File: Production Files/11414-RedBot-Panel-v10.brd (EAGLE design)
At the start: 94 x 49.5 mm, 66 parts, among them U1 ATMEGA328P, U2 TB6612FNG, U3 MIC5219 5V, U4 MIC5219 3.3V, U5 FT232RLSSOP, U6 7408SE, Y1 16MHz

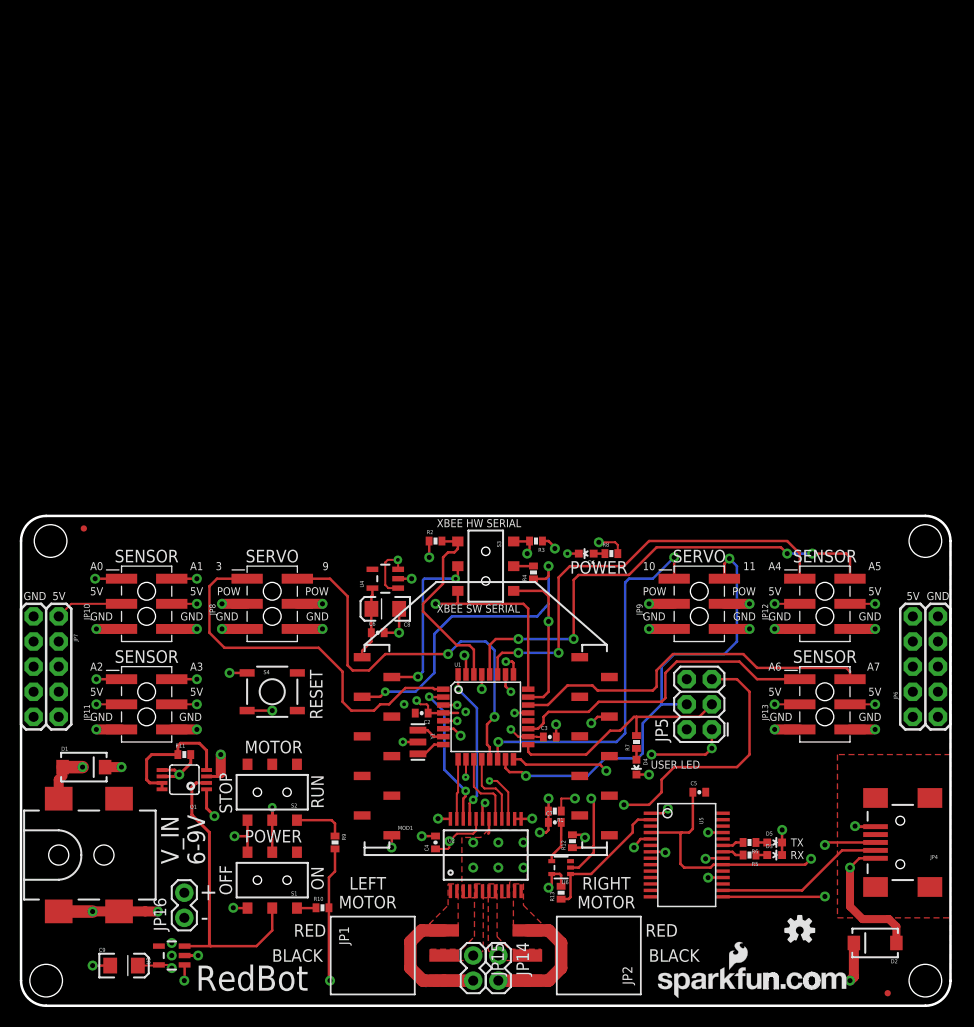
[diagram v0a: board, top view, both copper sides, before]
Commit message: Production readied
add fiducials & create panel
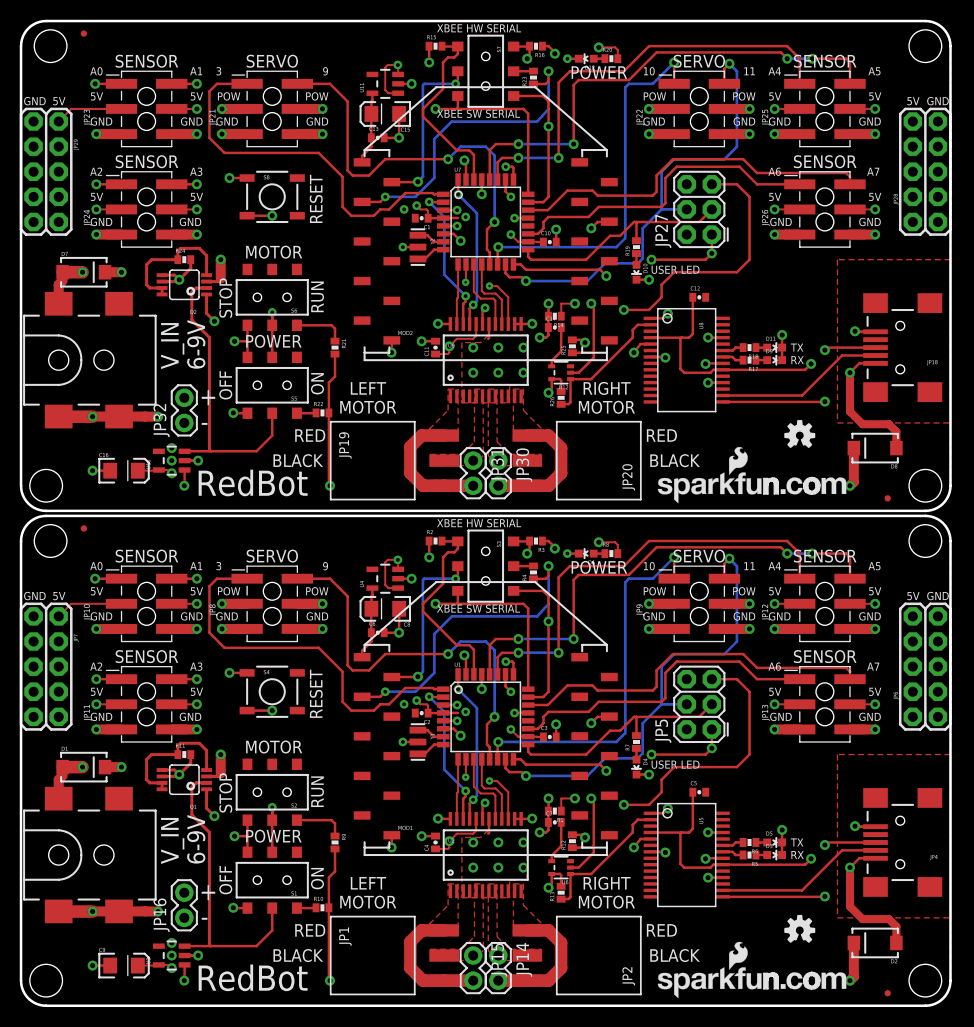
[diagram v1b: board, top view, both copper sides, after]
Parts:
- removed FRAME1: FRAME-LETTER, SparkFun-Aesthetics:CREATIVE_COMMONS
- added C1, C10, C11, C12, C13, C14: 0.1uF, SparkFun-Capacitors:0402-CAP
- added C15, C16: 10uF, SparkFun-Capacitors:EIA3216
- added D10, D11, D12, D9: GREEN, SparkFun-LED:LED-0603
- added D7, D8: (no value), SparkFun-DiscreteSemi:SMA-DIODE
- added FID3, FID4: FIDUCIALUFIDUCIAL, SparkFun-Aesthetics:MICRO-FIDUCIAL
- added JP17: 5.5x2.1mm Barrel, SparkFun-Connectors:POWER_JACK_SMD
- added JP18: USB-B, SparkFun-Connectors:USB-MINIB
- added JP19, JP20: 1x3 RA Female .1", SparkFun-Connectors:1X03_SMD_RA_FEMALE
- added JP21, JP22, JP23, JP24, JP25, JP26: (no value), SparkFun-Connectors:2X3_SMT_POSTS
- added JP27: AVR_SPI_PRG_6PTH, SparkFun-Connectors:2X3
- added JP28, JP29: M05X2NO_SILK, SparkFun-Connectors:2X5_NOSILK
- added JP30, JP31, JP32: (no value), SparkFun-Connectors:1X02
- added MOD2: XBEE-1B3, SparkFun-RF:XBEE-SMD
- added Q2: (no value), SparkFun-DiscreteSemi:MSOP8
- added R14, R21, R22, R24, R25, R26: 10k, SparkFun-Resistors:0402-RES
- added R15, R16, R17, R18, R19, R20, R23: 1k, SparkFun-Resistors:0402-RES
- added S5, S6, S7: DPDT, SparkFun-Electromechanical:AYZ0202
- added S8: (no value), SparkFun-Electromechanical:TACTILE_SWITCH_SMD
- added SFE-LOGO2: LOGO-SFENEW, SparkFun-Aesthetics:SFE-NEW-WEBLOGO
- added STANDOFF5, STANDOFF6, STANDOFF7, STANDOFF8: STAND-OFF, SparkFun-Electromechanical:STAND-OFF
- added U$1: OSHW-LOGOS, SparkFun-Aesthetics:OSHW-LOGO-S
- added U10: MIC5219 5V, SparkFun-PowerIC:SOT23-5
- added U11: MIC5219 3.3V, SparkFun-PowerIC:SOT23-5
- added U12: 7408SE, SparkFun-DigitalIC:SOT353
- added U7: ATMEGA328P, SparkFun-DigitalIC:TQFP32-08
- added U8: FT232RLSSOP, SparkFun-DigitalIC:SSOP28DB
- added U9: TB6612FNG, SparkFun-PowerIC:SSOP24
- added Y2: 16MHz, SparkFun-FreqCtrl:RESONATOR-SMD
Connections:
- new net 3.3V1: C13.1, C15.A, MOD2.1, U11.5
- new net 5V1: C1.1, C10.1, C11.1, C16.A, JP23.3, JP23.4, JP24.3, JP24.4, JP25.3, JP25.4, JP26.3, JP26.4, JP27.2, JP28.1, JP28.3, JP28.5, JP28.7, JP28.9, JP29.1, JP29.3, JP29.5, JP29.7, JP29.9, R14.1, R20.2, R25.2, R26.2, U10.5, U11.1, U11.3, U12.5, U7.18, U7.4, U7.6, U9.20
- new net AREF1: U7.20
- new net FT232_RXI1: R16.1, U8.5
- new net FT232_TXO1: R15.1, U8.1
- new net FTDI_DTR1: R26.1, U12.1, U8.2
- new net GND1: C1.2, C10.2, C11.2, C12.2, C13.2, C15.C, C16.C, D10.C, D11.C, D12.C, D9.C, JP17.GND, JP17.P$4, JP18.GND, JP21.5, JP21.6, JP22.5, JP22.6, JP23.5, JP23.6, JP24.5, JP24.6, JP25.5, JP25.6, JP26.5, JP26.6, JP27.6, JP28.10, JP28.2, JP28.4, JP28.6, JP28.8, JP29.10, JP29.2, JP29.4, JP29.6, JP29.8, JP32.1, MOD2.10, Q2.1, S5.3, S5.6, S6.3, S8.1, U10.2, U11.2, U12.3, U7.21, U7.3, U7.5, U8.18, U8.21, U8.25, U8.26, U8.7, U9.10, U9.18, U9.3, U9.4, U9.9, Y2.2
- new net L03: JP19.1, JP19.3, JP31.2, U9.1, U9.2
- new net L04: JP19.2, JP31.1, U9.5, U9.6
- new net L_CTRL_3: U7.2, U9.22
- new net L_CTRL_4: U7.32, U9.21
- new net MISO1: JP27.1, U7.16
- new net MOTOR_ENABLE1: S5.5, S6.2, U9.19
- new net N$10: JP18.D+, U8.15
- new net N$11: U7.8, Y2.3
- new net N$12: U7.7, Y2.1
- new net N$13: D11.A, R18.1
- new net N$14: D9.A, R17.1
- new net N$15: D10.A, R19.1
- new net N$16: D12.A, R20.1
- new net N$17: R21.1, S6.1
- new net N$19: C14.2, U12.4
- new net N$20: R23.2, S7.2
- new net N$21: JP18.MTN1, JP18.MTN2, JP18.MTN3, JP18.MTN4
- new net N$22: Q2.4, Q2.7, Q2.8, R24.1
- new net N$9: JP18.D-, U8.16
- new net PG_EN1: R22.1, S5.1
- new net PROGRAM_ENABLE1: Q2.2, S5.2, U10.3
- new net PWML1: U7.9, U9.23
- new net PWMR1: U7.10, U9.15
- new net R03: JP20.2, JP30.1, U9.7, U9.8
- new net R04: JP20.1, JP20.3, JP30.2, U9.11, U9.12
- new net RESET1: C14.1, JP27.5, R14.2, S8.3, U7.29
- new net RXI1: R15.2, S7.4, U7.30
- new net RXLED1: R17.2, U8.22
- new net R_CTRL_3: U7.11, U9.17
- new net R_CTRL_4: U7.12, U9.16
- new net SCK1: JP27.3, R19.2, U7.17
- new net SENSOR_0/SW_TXO1: JP23.1, S7.3, U7.23
- new net SENSOR_1: JP24.1, U7.25
- new net SENSOR_1/SW_RXI1: JP23.2, S7.6, U7.24
- new net SENSOR_10: JP25.2, U7.28
- new net SENSOR_11: JP26.1, U7.19
- new net SENSOR_12: JP26.2, U7.22
- new net SENSOR_8: JP24.2, U7.26
- new net SENSOR_9: JP25.1, U7.27
- new net SERVO_4: JP21.1, U7.1
- new net SERVO_4/MOSI1: JP22.2, JP27.4, U7.15
- new net SERVO_5: JP21.2, U7.13
- new net SERVO_6: JP22.1, U7.14
- new net TXLED1: R18.2, U8.23
- new net TXO1: R16.2, S7.1, U7.31
- new net V_BATT1: D7.A, JP17.VIN0, JP32.2, Q2.5, Q2.6, R24.2, U9.13, U9.14, U9.24
- new net V_GATED1: JP21.3, JP21.4, JP22.3, JP22.4, Q2.3
- new net V_IN1: D7.C, D8.C, R21.2, R22.2, U10.1
- new net V_USB1: C12.1, D8.A, JP18.VBUS, U8.20, U8.4
- new net XBEE_DIO1: MOD2.17, R25.1, U12.2
- new net XBEE_RXI1: MOD2.3, R23.1
- new net XBEE_TXO1: MOD2.2, S7.5
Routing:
- net V_IN1: track 0.00 -> 118.8 mm, vias 0 -> 4
- net V_GATED1: track 0.00 -> 113.8 mm, vias 0 -> 5
- net GND1: track 0.00 -> 84.7 mm, vias 0 -> 44
- net RESET1: track 0.00 -> 84.4 mm, vias 0 -> 5
- net V_BATT1: track 0.00 -> 80.8 mm, vias 0 -> 4
- net SENSOR_0/SW_TXO1: track 0.00 -> 69.5 mm, vias 0 -> 2
- net 5V1: track 0.00 -> 62.1 mm, vias 0 -> 20
- net FT232_TXO1: track 0.00 -> 50.2 mm, vias 0 -> 2
- net SENSOR_10: track 0.00 -> 49.6 mm, vias 0 -> 4
- net SENSOR_1/SW_RXI1: track 0.00 -> 47.8 mm, vias 0 -> 2
- net SERVO_4/MOSI1: track 0.00 -> 47.7 mm, vias 0 -> 2
- net SENSOR_1: track 0.00 -> 47.1 mm, vias 0 -> 2
- net SENSOR_9: track 0.00 -> 44.7 mm, vias 0 -> 2
- net V_USB1: track 0.00 -> 43.5 mm, vias 0 -> 2
- net FT232_RXI1: track 0.00 -> 43.4 mm, vias 0 -> 2
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- added copper zone on layer 2, net 5V1
- added copper zone on layer 1, net GND1
- added copper zone on layer 15, net GND1
- added copper zone on layer 16, net GND1
- added copper zone on layer 1, net L03
- added copper zone on layer 1, net L04
- added copper zone on layer 1, net N$21
- added copper zone on layer 1, net R03
- added copper zone on layer 1, net R04
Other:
- board size 94 x 49.5 mm -> 94 x 99.6 mm
- board text removed: "M. Hord"
